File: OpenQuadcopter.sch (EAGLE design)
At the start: 78 parts, among them U1 MPU-6000QFN-24

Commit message: Fixed.
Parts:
- C10, C18, C22, C23: value (none) -> 100nF
- C13, C14, C16, C21: value (none) -> 4.7uF; device openmotestm:C-EUC0402 -> openmotestm:C-EUC0603
- C15, C20: value (none) -> 15pF
- C17, C19: value (none) -> 10nF
- C24: value (none) -> 1uF
- C8: value (none) -> 10uF; device openmotestm:C-EUC0402 -> openmotestm:C-EUC0603
- R1, R11, R2, R21, R22, R24, R25, R3, R4, R9: value (none) -> 10K
- R10, R8: value (none) -> 1.2K
- R12: value (none) -> 10R
- R13: value (none) -> 39K
- R14, R16: value (none) -> 30K
- R15: value (none) -> 42.2K
- R17: value (none) -> 150K
- R18: value (none) -> 300K
- R19, R20: value (none) -> 1K
- R23: value (none) -> 100K
- R26: value (none) -> 20K
- R27, R28: value (none) -> 0R
- U$1: value HMC5883LSMD -> HMC5883L-SMD
- U$2, U$4, U$6, U$8: value MOSFET -> PWV31XN
- U1: value MPU-6000QFN-24 -> MPU-6050QFN-24
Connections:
- net DGND: now also C21.2; no longer C21.1
- net VCCD: now also C21.1; no longer C21.2
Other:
- moved on the sheet: C21

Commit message: update PB6
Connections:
- net SDL/PB6 renamed SCL/PB6
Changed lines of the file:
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@@
-</segment>
-</net>
-<net name="SDL/PB6" class="0">
-<segment>
-<pinref part="U$11" gate="G$1" pin="DIO11"/>
-<wire x1="109.22" y1="78.74" x2="93.98" y2="78.74" width="0.1524" layer="91"/>
-<label x="93.98" y="78.74" size="1.778" layer="95"/>
-</segment>
-<segment>
-<pinref part="U1" gate="G$1" pin="SCL/SCLK"/>
-<wire x1="-33.02" y1="88.9" x2="-17.78" y2="88.9" width="0.1524" layer="91"/>
-<label x="-27.94" y="88.9" size="1.778" layer="95"/>
 </segment>
 </net>
@@
 </segment>
 </net>
+<net name="SCL/PB6" class="0">
+<segment>
+<pinref part="U$11" gate="G$1" pin="DIO11"/>
+<wire x1="109.22" y1="78.74" x2="93.98" y2="78.74" width="0.1524" layer="91"/>
+<label x="93.98" y="78.74" size="1.778" layer="95"/>
+</segment>
+<segment>
+<pinref part="U1" gate="G$1" pin="SCL/SCLK"/>
+<wire x1="-33.02" y1="88.9" x2="-17.78" y2="88.9" width="0.1524" layer="91"/>
+<label x="-27.94" y="88.9" size="1.778" layer="95"/>
+</segment>
+</net>

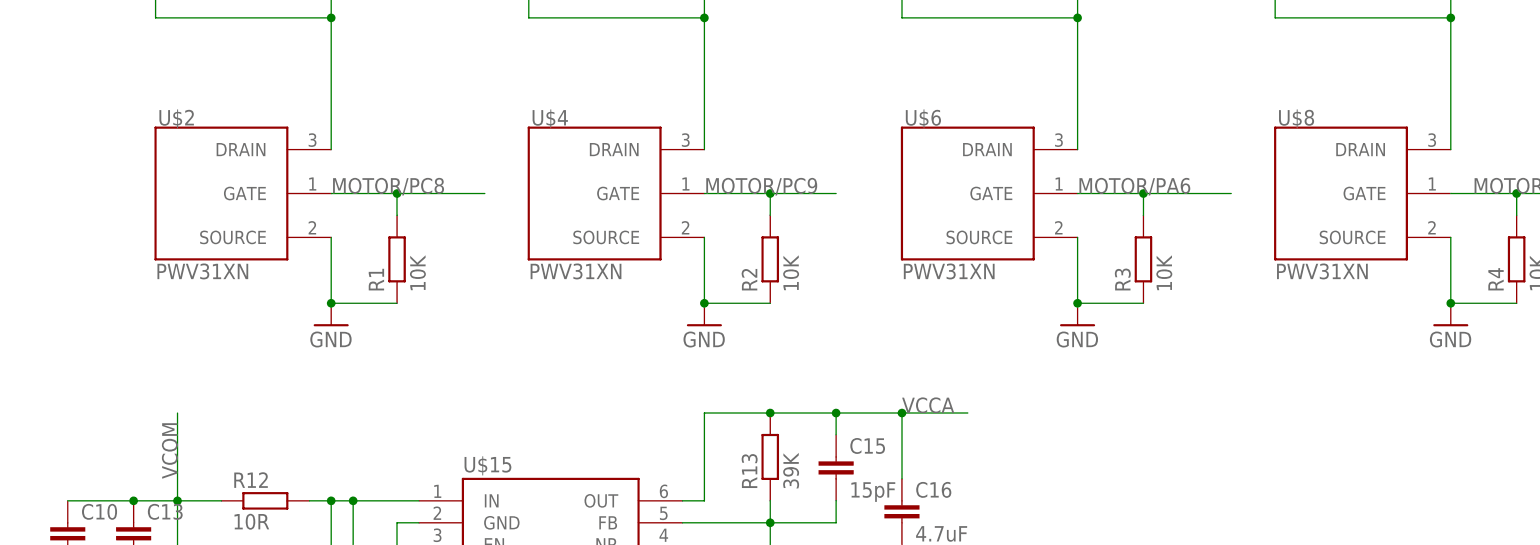
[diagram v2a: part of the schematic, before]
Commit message: Correct the name PMV31XN.
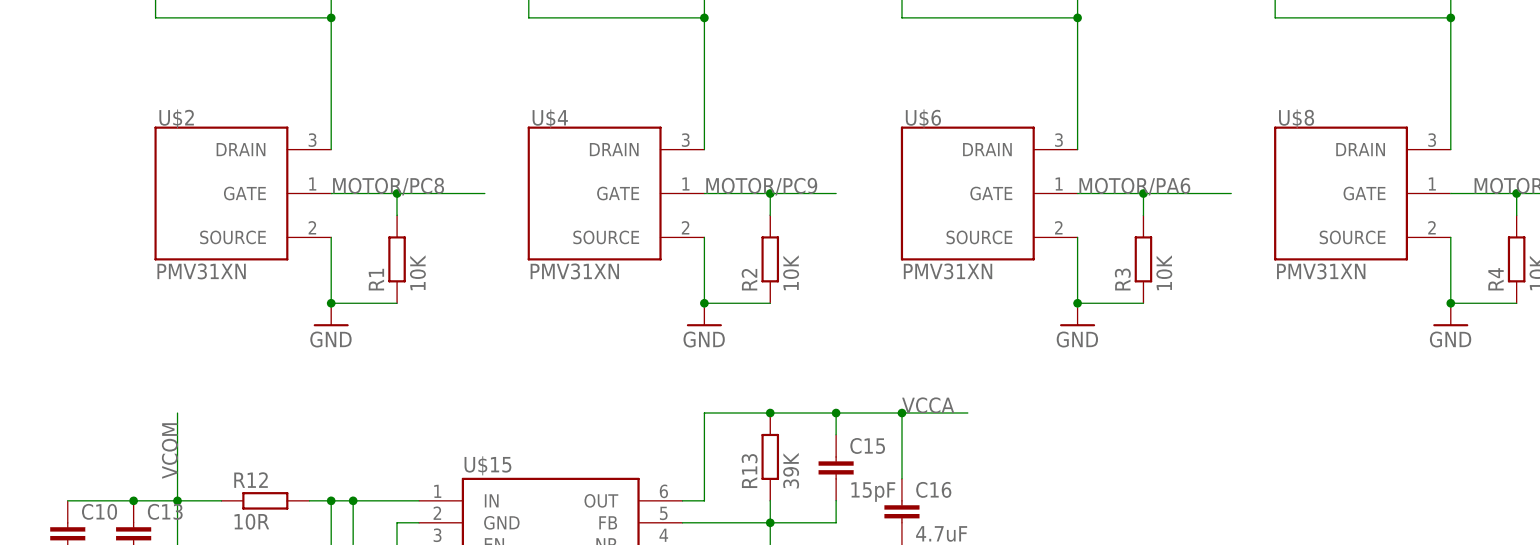
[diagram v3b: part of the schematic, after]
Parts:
- U$2, U$4, U$6, U$8: value PWV31XN -> PMV31XN
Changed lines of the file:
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@@
 <part name="U1" library="openmotestm" deviceset="MPU-6000" device="QFN-24" value="MPU-6050QFN-24"/>
 <part name="U$1" library="openmotestm" deviceset="HMC5883L" device="SMD" value="HMC5883L-SMD"/>
-<part name="U$2" library="openmotestm" deviceset="MOSFET" device="" value="PWV31XN"/>
+<part name="U$2" library="openmotestm" deviceset="MOSFET" device="" value="PMV31XN"/>
 <part name="U$11" library="openmotestm" deviceset="XBEE-1" device="B3"/>
 <part name="U$12" library="openmotestm" deviceset="SWITCH_SPDT" device=""/>
@@
 <part name="D1" library="diode" deviceset="BAT54" device=""/>
 <part name="R1" library="rcl" deviceset="R-EU_" device="R0402" value="10K"/>
-<part name="U$4" library="openmotestm" deviceset="MOSFET" device="" value="PWV31XN"/>
+<part name="U$4" library="openmotestm" deviceset="MOSFET" device="" value="PMV31XN"/>
 <part name="U$5" library="openmotestm" deviceset="MOTOR" device="10MM" value="MOTOR"/>
 <part name="GND2" library="supply1" deviceset="GND" device=""/>
 <part name="D2" library="diode" deviceset="BAT54" device=""/>
 <part name="R2" library="rcl" deviceset="R-EU_" device="R0402" value="10K"/>
-<part name="U$6" library="openmotestm" deviceset="MOSFET" device="" value="PWV31XN"/>
+<part name="U$6" library="openmotestm" deviceset="MOSFET" device="" value="PMV31XN"/>
 <part name="U$7" library="openmotestm" deviceset="MOTOR" device="10MM" value="MOTOR"/>
 <part name="GND3" library="supply1" deviceset="GND" device=""/>
 <part name="D3" library="diode" deviceset="BAT54" device=""/>
 <part name="R3" library="rcl" deviceset="R-EU_" device="R0402" value="10K"/>
-<part name="U$8" library="openmotestm" deviceset="MOSFET" device="" value="PWV31XN"/>
+<part name="U$8" library="openmotestm" deviceset="MOSFET" device="" value="PMV31XN"/>
 <part name="U$9" library="openmotestm" deviceset="MOTOR" device="10MM" value="MOTOR"/>
 <part name="GND4" library="supply1" deviceset="GND" device=""/>

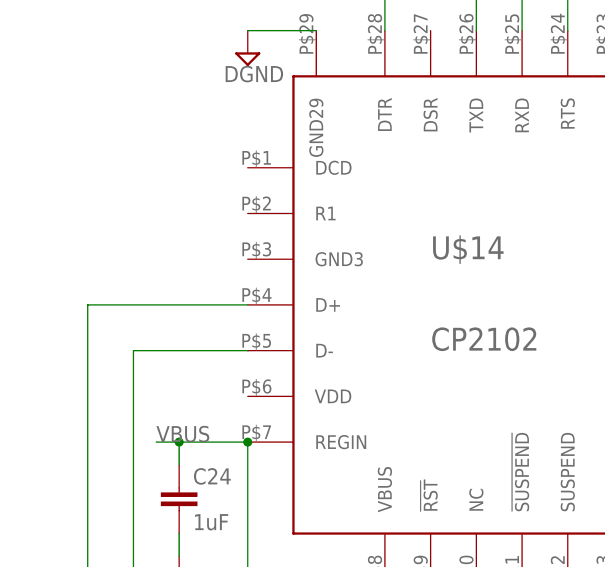
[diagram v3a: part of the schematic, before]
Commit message: add 0.1uF capacitor between VDD and GND pin of CP2102.
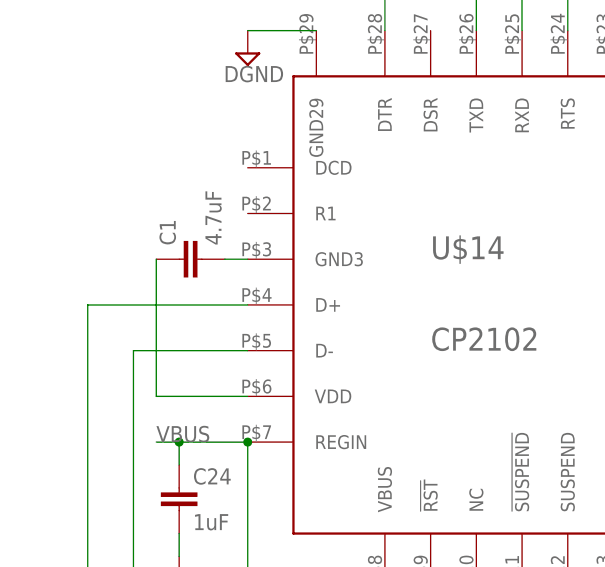
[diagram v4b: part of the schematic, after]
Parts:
- added C1: 4.7uF, openmotestm:C-EUC0402
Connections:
- new net N$10: C1.2, U$14.GND3
- new net N$17: C1.1, U$14.VDD
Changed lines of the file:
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@@
 <?xml version="1.0" encoding="utf-8"?>
 <!DOCTYPE eagle SYSTEM "eagle.dtd">
-<eagle version="6.6.0">
+<eagle version="7.5.0">
 <drawing>
 <settings>
@@
 <part name="C16" library="openmotestm" deviceset="C-EU" device="C0603" value="4.7uF"/>
 <part name="C21" library="openmotestm" deviceset="C-EU" device="C0603" value="4.7uF"/>
+<part name="C1" library="openmotestm" deviceset="C-EU" device="C0402" value="4.7uF"/>
 </parts>
 <sheets>
@@
 <instance part="C16" gate="G$1" x="-5.08" y="-35.56"/>
 <instance part="C21" gate="G$1" x="15.24" y="-71.12"/>
+<instance part="C1" gate="G$1" x="-182.88" y="20.32" rot="R90"/>
 </instances>
 <busses>
@@
 </segment>
 </net>
+<net name="N$10" class="0">
+<segment>
+<pinref part="U$14" gate="G$1" pin="GND3"/>
+<pinref part="C1" gate="G$1" pin="2"/>
+<wire x1="-175.26" y1="20.32" x2="-177.8" y2="20.32" width="0.1524" layer="91"/>
+</segment>
+</net>
+<net name="N$17" class="0">
+<segment>
+<pinref part="U$14" gate="G$1" pin="VDD"/>
+<pinref part="C1" gate="G$1" pin="1"/>
+<wire x1="-175.26" y1="5.08" x2="-185.42" y2="5.08" width="0.1524" layer="91"/>
+<wire x1="-185.42" y1="5.08" x2="-185.42" y2="20.32" width="0.1524" layer="91"/>
+</segment>
+</net>

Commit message: fixed.
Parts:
- C1: value 4.7uF -> 0.1uF
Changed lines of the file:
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@@
 <part name="C16" library="openmotestm" deviceset="C-EU" device="C0603" value="4.7uF"/>
 <part name="C21" library="openmotestm" deviceset="C-EU" device="C0603" value="4.7uF"/>
-<part name="C1" library="openmotestm" deviceset="C-EU" device="C0402" value="4.7uF"/>
+<part name="C1" library="openmotestm" deviceset="C-EU" device="C0402" value="0.1uF"/>
 </parts>
 <sheets>
